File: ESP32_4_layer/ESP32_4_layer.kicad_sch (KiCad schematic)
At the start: 27 parts, among them J1 SS-52400-003, J2 JST_S2B-PH-K-S_LF__SN_, U1 MCP73871-4CC

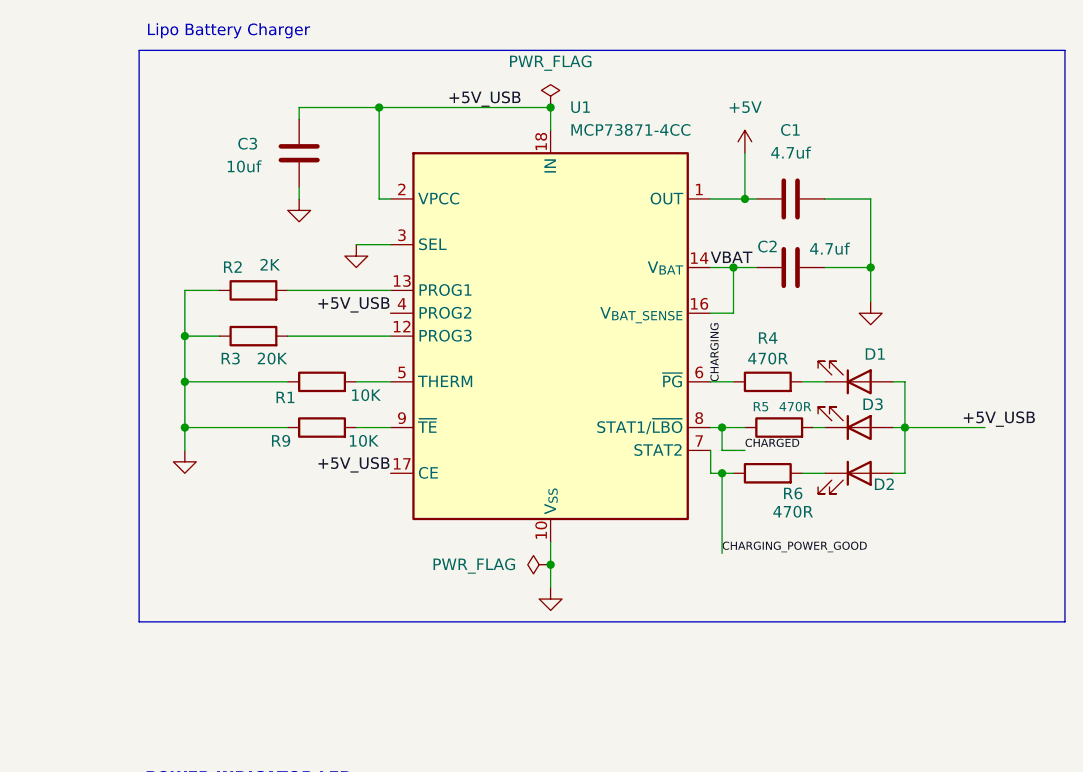
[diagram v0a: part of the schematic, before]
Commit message: upto inner layer copper zone
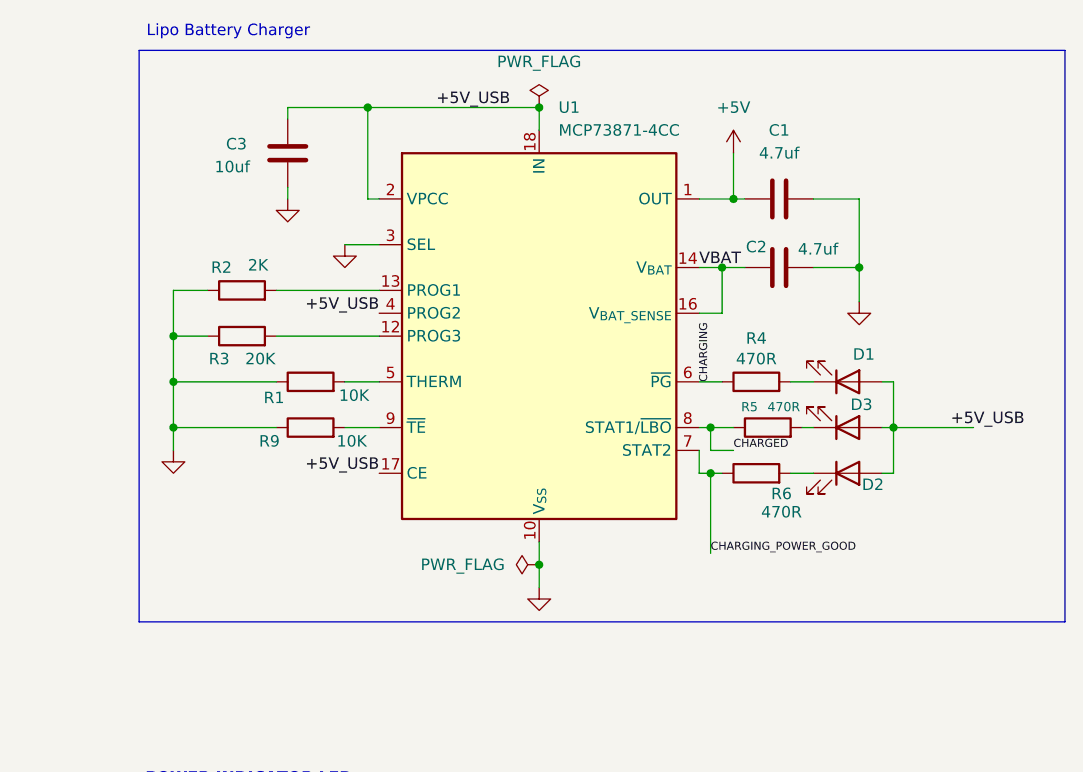
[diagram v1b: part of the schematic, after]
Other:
- moved on the sheet: C1, C2, C3, D1, D2, D3, R1, R2, R3, R4, R5, R6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
